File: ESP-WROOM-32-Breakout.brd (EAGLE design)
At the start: 35.1 x 45.4 mm, 29 parts, among them U3 ESP-WROOM-32

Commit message: Add files via upload
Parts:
- removed R5: 150K, hari:0402
- removed R6: 47K, hari:0402
- added R8: 150K, rcl:R0603
- added R9: 47K, rcl:R0603
- moved C3 1.40 mm to (6.60, 37.2)
- moved C8 1.30 mm to (5.17, 37.3)
- moved R2 0.30 mm to (2.24, 40.6)
- moved C10 0.10 mm to (13.4, 15.9)
- moved C4 0.10 mm to (11.9, 15.9)
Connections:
- net GND: now also R9.1; no longer R6.1
- net N$4: now also R8.2, R9.2; no longer R5.2, R6.2
- net VCC: now also R8.1; no longer R5.1
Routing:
- net VCC: track 16.0 -> 18.2 mm
- net EN: track 62.9 -> 63.9 mm
- net GND: track 5.44 -> 5.13 mm, vias 19 -> 28
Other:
- board size 35.1 x 45.4 mm -> 35.1 x 45.8 mm
- board text added: "En"
- board text added: "VIN"
- board text removed: "E"
- board text removed: "VB"

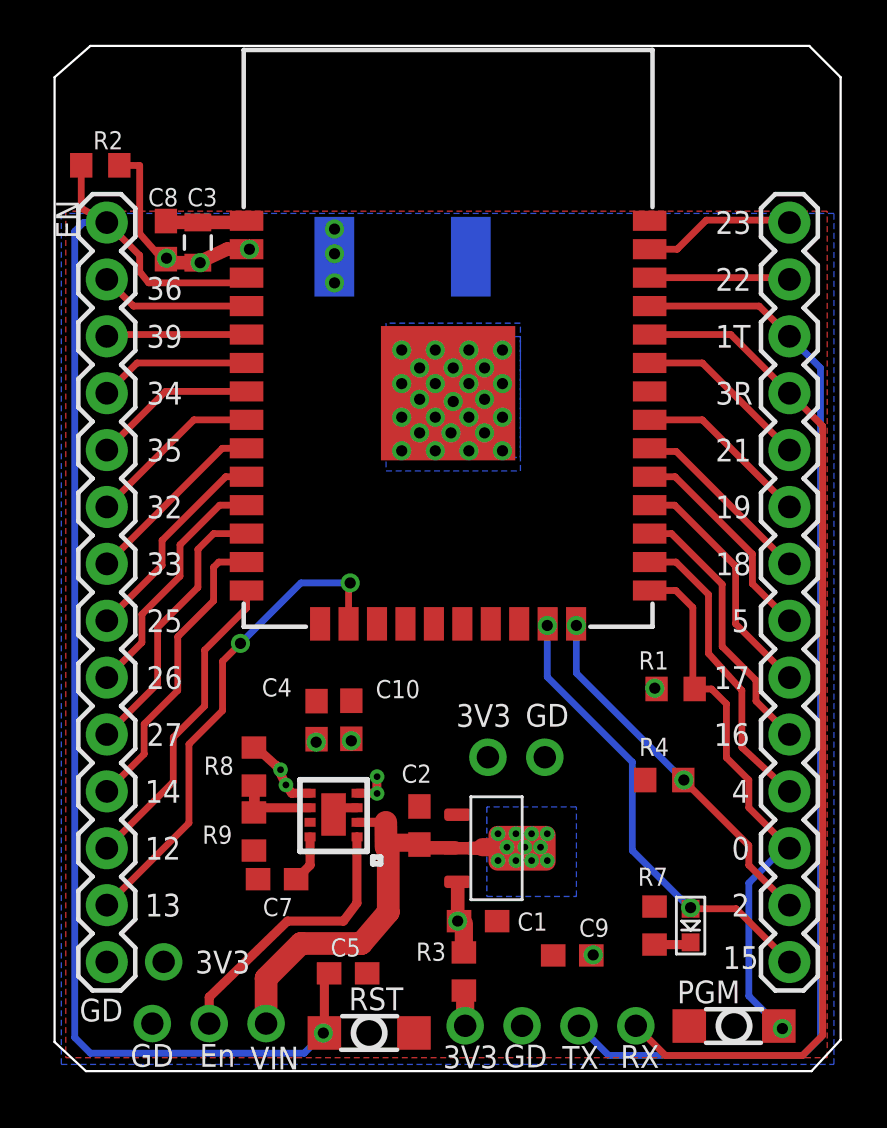
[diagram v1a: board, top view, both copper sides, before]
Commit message: pinout silkscreen on bottom, wider traces
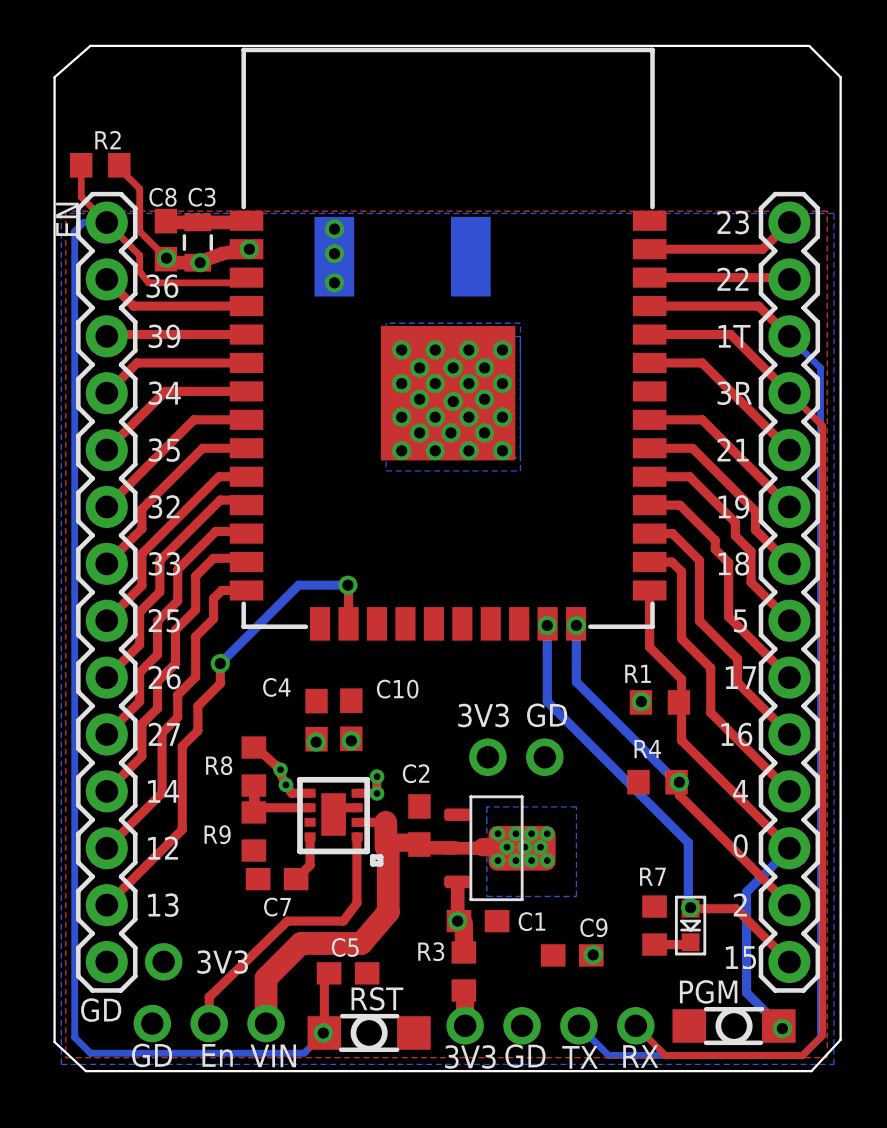
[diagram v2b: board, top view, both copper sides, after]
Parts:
- moved R1 0.92 mm to (27.2, 16.7)
- moved R4 0.32 mm to (27.1, 13.1)
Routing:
- net TXD0: track 50.4 -> 51.5 mm
- net IO0: track 24.8 -> 23.8 mm
- net IO12: track 14.1 -> 14.7 mm
- net VCC: track 18.2 -> 17.6 mm
- net IO33: track 8.38 -> 8.89 mm

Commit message: Add files via upload
moved led to pin 13, changed cap package C11 (now can accomodate tantalum B size e.g. 220uf 4V), remove thermals on some footprints for contiguous ground plane
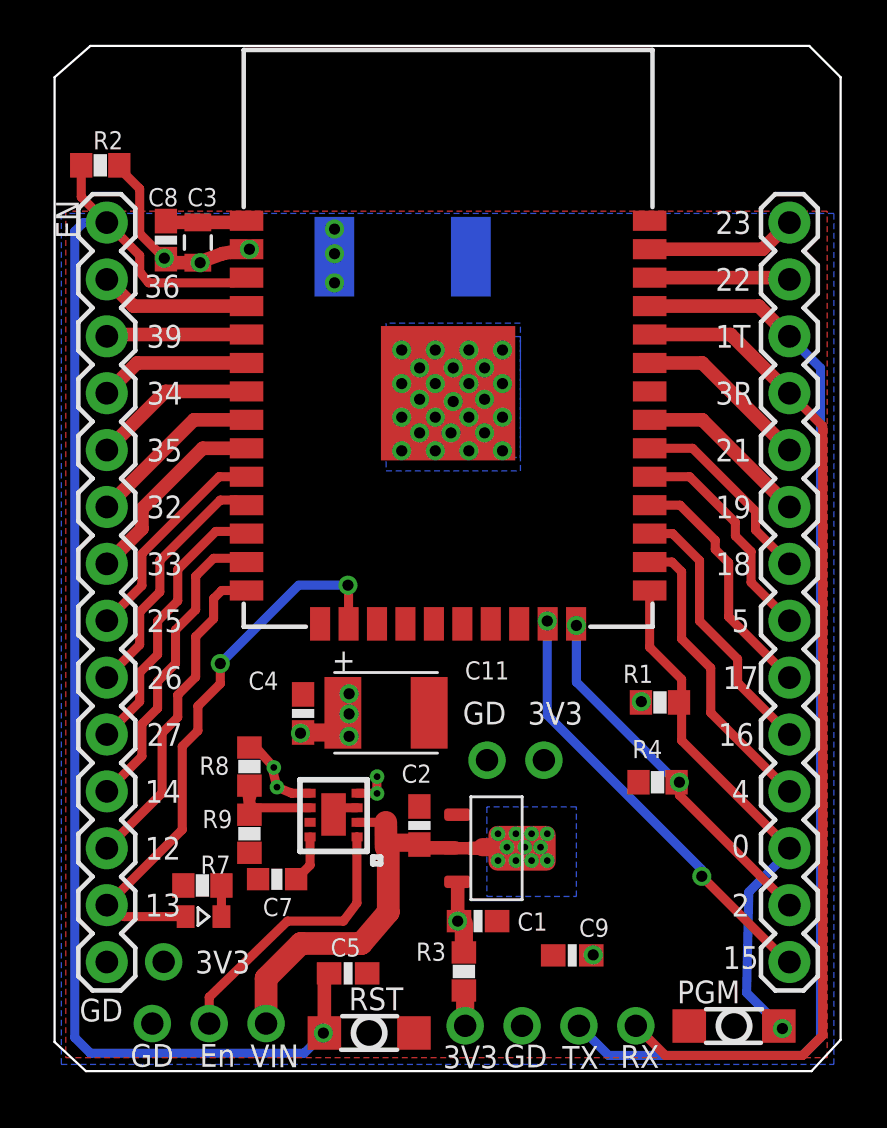
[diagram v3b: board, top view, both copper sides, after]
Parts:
- removed C10: 10u, rcl:C0603
- added C11: (no value), SparkFun-Passives:GRM43D
- moved LED1 21.8 mm to (6.80, 7.10), turned to 270 degrees
- moved R7 20.3 mm to (6.80, 8.49), turned to 0 degrees
- moved C4 0.67 mm to (11.3, 16.2)
- moved R9 0.22 mm to (8.90, 10.8)
- moved R8 0.20 mm to (8.90, 13.8)
- moved JP3 0.14 mm to (20.8, 14.1), turned to 180 degrees
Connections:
- net GND: now also C11.C; no longer C10.2
- net IO13: now also LED1.A
- net IO15: no longer LED1.A
- net VCC: now also C11.A; no longer C10.1
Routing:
- net IO13: track 21.8 -> 25.4 mm
- net VCC: track 17.6 -> 19.9 mm, vias 12 -> 14
- net IO15: track 20.6 -> 19.8 mm
- net N$4: track 4.16 -> 5.04 mm
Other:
- board text added: "+"
